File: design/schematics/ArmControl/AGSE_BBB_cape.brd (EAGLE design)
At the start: 71.8 x 54.6 mm, 53 parts, among them Q1 PFET-FQP27P06, Q2 PFET-FQP27P06, Q3 NFET-FQP30N06L, Q4 NFET-FQP30N06L, Q5 PFET-FQP27P06, Q6 PFET-FQP27P06, Q7 NFET-FQP30N06L, Q8 NFET-FQP30N06L, U1 V_REG_LD1085D2

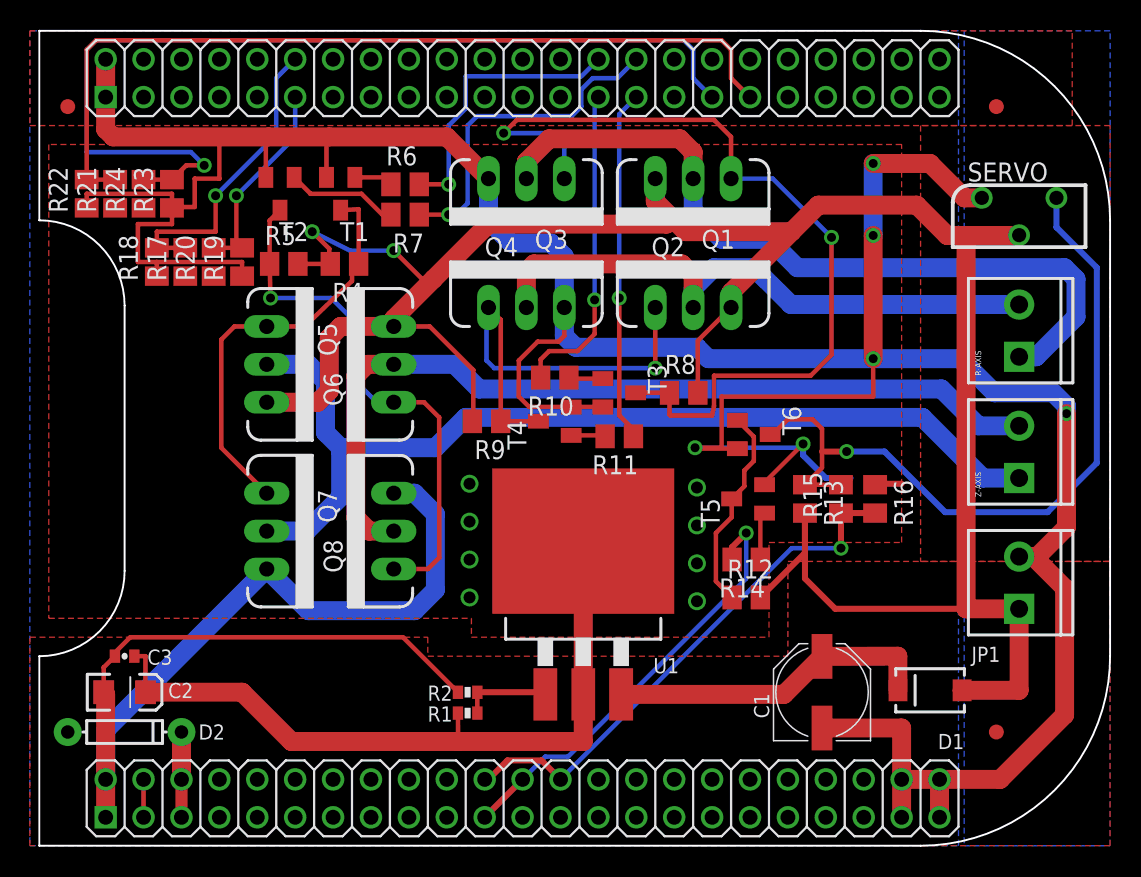
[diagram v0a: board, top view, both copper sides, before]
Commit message: routed the board.  Missing the encoder connectors.
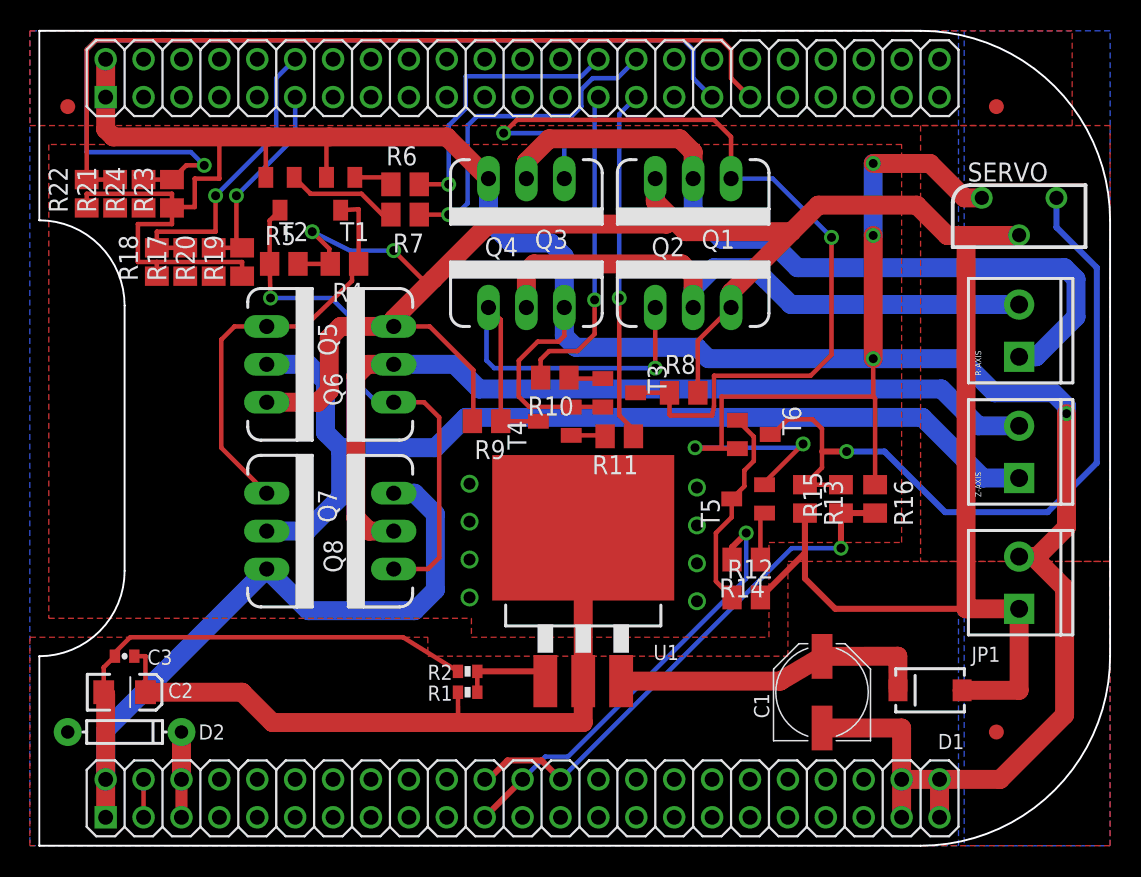
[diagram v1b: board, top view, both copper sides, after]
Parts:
- moved R1 1.40 mm to (45.8, 12.8)
- moved R2 1.40 mm to (45.8, 14.2)
- moved U1 0.89 mm to (53.6, 21.8)
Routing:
- net GND: track 325.6 -> 324.5 mm
- net VOUT: track 49.2 -> 48.4 mm
- net N$3: track 21.9 -> 21.3 mm
- net N$4: track 6.10 -> 6.61 mm
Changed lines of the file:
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@@
 <elements>
 <element name="U$1" library="adafruit" package="BEAGLEBONE_SHIELD" value="BEAGLEBONE_OUTLINE" x="2.54" y="57.15" smashed="yes" rot="R270"/>
-<element name="U1" library="SparkFun-PowerIC" package="D2PACK/A" value="V_REG_LD1085D2" x="53.594" y="20.955" smashed="yes">
-<attribute name="MANEX" value="140-0004281" x="53.594" y="20.955" size="1.778" layer="27" display="off"/>
-<attribute name="NAME" x="58.293" y="14.097" size="1.016" layer="25"/>
+<element name="U1" library="SparkFun-PowerIC" package="D2PACK/A" value="V_REG_LD1085D2" x="53.594" y="21.844" smashed="yes">
+<attribute name="MANEX" value="140-0004281" x="53.594" y="21.844" size="1.778" layer="27" display="off"/>
+<attribute name="NAME" x="58.293" y="14.986" size="1.016" layer="25"/>
 </element>
 <element name="JP1" library="SparkFun-Connectors" package="SCREWTERMINAL-3.5MM-2" value="M023.5MM" x="82.804" y="18.415" smashed="yes" rot="R90">
@@
 <attribute name="VALUE" x="21.844" y="8.763" size="0.4064" layer="27"/>
 </element>
-<element name="R1" library="SparkFun-Passives" package="0402-RES" value="370" x="45.847" y="11.43" smashed="yes" rot="R180">
-<attribute name="MANEX" value="110-0003316" x="45.847" y="11.43" size="1.778" layer="27" rot="R180" display="off"/>
-<attribute name="NAME" x="44.831" y="11.8745" size="1.016" layer="25" rot="R180"/>
-</element>
-<element name="R2" library="SparkFun-Passives" package="0402-RES" value="1.5k" x="45.847" y="12.827" smashed="yes">
-<attribute name="MANEX" value="110-0001936" x="45.847" y="12.827" size="1.778" layer="27" display="off"/>
+<element name="R1" library="SparkFun-Passives" package="0402-RES" value="370" x="45.847" y="12.827" smashed="yes" rot="R180">
+<attribute name="MANEX" value="110-0003316" x="45.847" y="12.827" size="1.778" layer="27" rot="R180" display="off"/>
 <attribute name="NAME" x="44.831" y="13.2715" size="1.016" layer="25" rot="R180"/>
+</element>
+<element name="R2" library="SparkFun-Passives" package="0402-RES" value="1.5k" x="45.847" y="14.224" smashed="yes">
+<attribute name="MANEX" value="110-0001936" x="45.847" y="14.224" size="1.778" layer="27" display="off"/>
+<attribute name="NAME" x="44.831" y="14.6685" size="1.016" layer="25" rot="R180"/>
 </element>
 <element name="FID1" library="SparkFun-Aesthetics" package="FIDUCIAL-1X2" value="FIDUCIAL1X2" x="19.05" y="52.07"/>
@@
 <wire x1="54.907" y1="31.943" x2="52.794" y2="31.943" width="0.3048" layer="1"/>
 <wire x1="52.794" y1="31.943" x2="52.789" y2="31.938" width="0.3048" layer="1"/>
-<wire x1="74.93" y1="26.797" x2="73.218" y2="26.797" width="0.4064" layer="1"/>
 <wire x1="73.218" y1="26.797" x2="73.152" y2="26.731" width="0.4064" layer="1"/>
 <wire x1="52.324" y1="38.608" x2="52.324" y2="42.037" width="1.27" layer="16"/>
@@
 <wire x1="21.59" y1="12.697" x2="21.59" y2="6.985" width="1.27" layer="1"/>
 <wire x1="21.59" y1="6.985" x2="21.59" y2="4.445" width="1.27" layer="1"/>
-<wire x1="45.197" y1="12.827" x2="41.514" y2="16.51" width="0.3048" layer="1"/>
+<wire x1="45.197" y1="14.224" x2="41.514" y2="16.51" width="0.3048" layer="1"/>
 <wire x1="41.514" y1="16.51" x2="23.241" y2="16.51" width="0.3048" layer="1"/>
 <wire x1="23.241" y1="16.51" x2="22.21" y2="15.479" width="0.3048" layer="1"/>
@@
 <wire x1="85.852" y1="11.303" x2="81.534" y2="6.985" width="1.27" layer="1"/>
 <wire x1="81.534" y1="6.985" x2="77.47" y2="6.985" width="1.27" layer="1"/>
-<wire x1="68.326" y1="29.464" x2="68.326" y2="28.702" width="0.4064" layer="16"/>
-<wire x1="68.326" y1="28.702" x2="69.85" y2="27.178" width="0.4064" layer="16"/>
-<wire x1="69.85" y1="27.178" x2="71.501" y2="27.178" width="0.4064" layer="16"/>
 <wire x1="80.304" y1="45.954" x2="79.141" y2="45.954" width="1.27" layer="1"/>
 <wire x1="79.141" y1="45.954" x2="76.835" y2="48.26" width="1.27" layer="1"/>
@@
 <wire x1="23.749" y1="44.196" x2="26.035" y2="44.196" width="0.3048" layer="1"/>
 <wire x1="26.035" y1="44.196" x2="26.035" y2="45.278" width="0.3048" layer="1"/>
-<wire x1="71.501" y1="27.178" x2="73.152" y2="26.731" width="0" layer="19" extent="1-16"/>
-<wire x1="42.291" y1="26.162" x2="49.276" y2="32.639" width="0" layer="19" extent="1-16"/>
+<wire x1="73.152" y1="26.731" x2="73.152" y2="32.512" width="0.3048" layer="1"/>
+<wire x1="73.152" y1="32.512" x2="73.025" y2="32.639" width="0.3048" layer="1"/>
 </signal>
 <signal name="N$3">
@@
 <wire x1="74.685" y1="12.954" x2="74.676" y2="15.24" width="1.27" layer="1"/>
 <wire x1="74.676" y1="15.24" x2="69.596" y2="15.227" width="1.27" layer="1"/>
-<wire x1="69.596" y1="15.227" x2="67.049" y2="12.68" width="1.27" layer="1"/>
-<wire x1="67.049" y1="12.68" x2="56.134" y2="12.68" width="1.27" layer="1"/>
+<wire x1="69.596" y1="15.227" x2="66.795" y2="13.569" width="1.27" layer="1"/>
+<wire x1="66.795" y1="13.569" x2="56.134" y2="13.569" width="1.27" layer="1"/>
 </signal>
 <signal name="5V">
@@
 <contactref element="U1" pad="1"/>
 <contactref element="R1" pad="1"/>
-<wire x1="46.497" y1="11.43" x2="46.497" y2="12.827" width="0.3048" layer="1"/>
-<wire x1="46.497" y1="12.827" x2="51.054" y2="12.827" width="0.4064" layer="1"/>
-<wire x1="51.054" y1="12.827" x2="51.054" y2="12.68" width="0.4064" layer="1"/>
+<wire x1="46.497" y1="12.827" x2="46.497" y2="14.224" width="0.3048" layer="1"/>
+<wire x1="46.497" y1="14.224" x2="51.054" y2="14.224" width="0.4064" layer="1"/>
+<wire x1="51.054" y1="14.224" x2="51.054" y2="13.569" width="0.4064" layer="1"/>
 </signal>
 <signal name="VOUT">
@@
 <contactref element="R1" pad="2"/>
 <contactref element="U1" pad="TAB"/>
-<wire x1="53.594" y1="12.68" x2="53.594" y2="22.955" width="1.27" layer="1"/>
+<wire x1="53.594" y1="13.569" x2="53.594" y2="23.844" width="1.27" layer="1"/>
 <via x="61.214" y="18.923" extent="1-16" drill="0.8"/>
 <via x="61.214" y="21.463" extent="1-16" drill="0.8"/>
@@
 <wire x1="24.26" y1="12.827" x2="24.257" y2="12.954" width="1.27" layer="1"/>
 <wire x1="24.26" y1="12.827" x2="30.734" y2="12.827" width="1.27" layer="1"/>
-<wire x1="30.734" y1="12.827" x2="34.036" y2="9.525" width="1.27" layer="1"/>
-<wire x1="34.036" y1="9.525" x2="45.212" y2="9.525" width="1.27" layer="1"/>
-<wire x1="45.212" y1="9.525" x2="53.594" y2="9.525" width="1.27" layer="1"/>
-<wire x1="53.594" y1="9.525" x2="53.594" y2="12.68" width="1.27" layer="1"/>
+<wire x1="30.734" y1="12.827" x2="32.766" y2="10.795" width="1.27" layer="1"/>
+<wire x1="32.766" y1="10.795" x2="45.212" y2="10.795" width="1.27" layer="1"/>
+<wire x1="45.212" y1="10.795" x2="53.594" y2="10.795" width="1.27" layer="1"/>
+<wire x1="53.594" y1="10.795" x2="53.594" y2="13.569" width="1.27" layer="1"/>
 <polygon width="0.3048" layer="1" thermals="no">
 <vertex x="17.78" y="49.53"/>
@@
 <vertex x="74.93" y="49.53"/>
 </polygon>
-<wire x1="45.197" y1="11.43" x2="45.212" y2="9.525" width="0.3048" layer="1"/>
+<wire x1="45.197" y1="12.827" x2="45.212" y2="10.795" width="0.3048" layer="1"/>
 <wire x1="23.51" y1="15.24" x2="24.257" y2="15.24" width="0.3048" layer="1"/>
 <wire x1="24.257" y1="15.24" x2="24.257" y2="12.954" width="0.3048" layer="1"/>

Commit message: routed the board, cleaned up the names and made ready for fab.
also added sparkfun's DRU for checking fab-ability
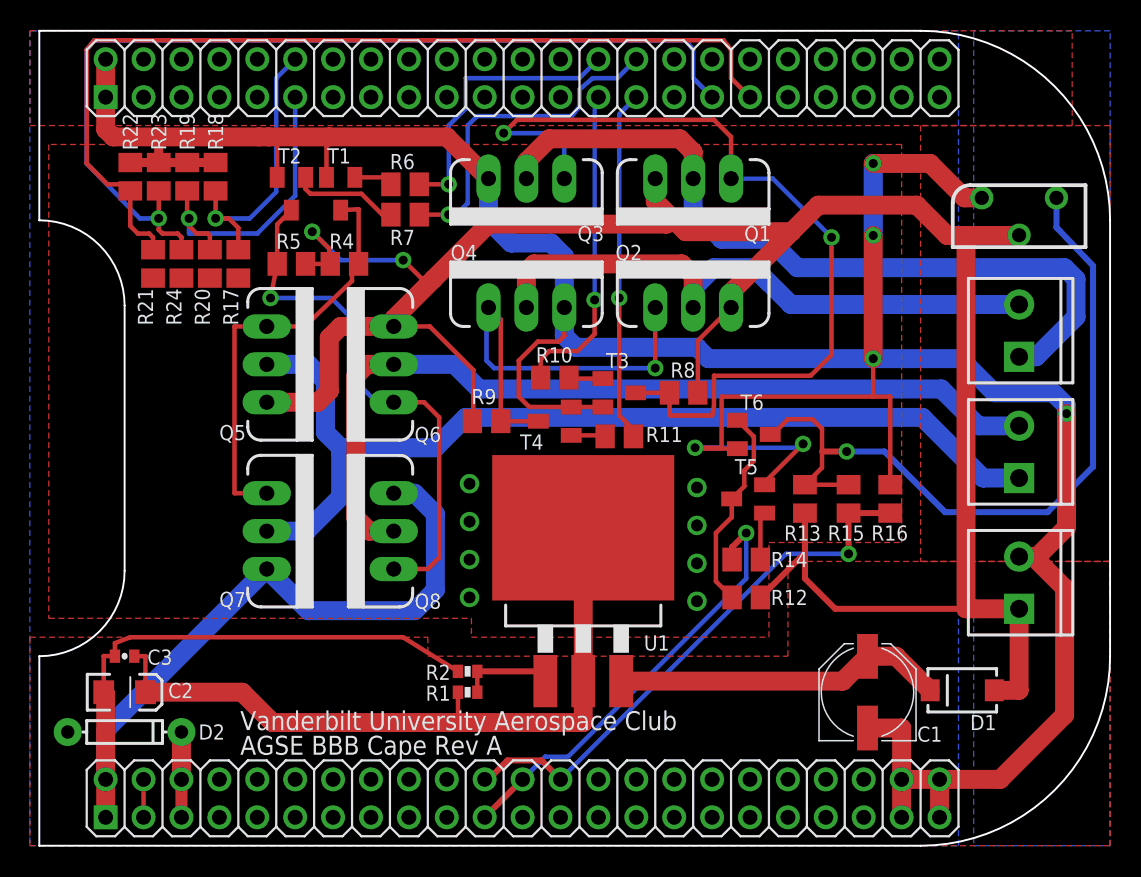
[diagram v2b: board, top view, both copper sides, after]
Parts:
- removed FID1, FID2, FID3: FIDUCIAL1X2, SparkFun-Aesthetics:FIDUCIAL-1X2
- moved R18 6.94 mm to (29.0, 47.4), turned to 270 degrees
- moved R19 6.80 mm to (27.1, 47.4), turned to 270 degrees
- moved R24 5.34 mm to (26.7, 41.5)
- moved R21 5.34 mm to (24.8, 41.5)
- moved R17 3.56 mm to (30.5, 41.5)
- moved R22 3.14 mm to (23.2, 47.4), turned to 270 degrees
- moved C1 3.05 mm to (72.6, 12.8)
- moved D1 2.16 mm to (79.0, 13.0)
- moved R23 1.45 mm to (25.1, 47.4), turned to 270 degrees
- moved R16 1.02 mm to (74.2, 25.8)
- moved T2 0.76 mm to (34.0, 46.2)
- moved R5 0.51 mm to (34.0, 41.5)
- moved R15 0.51 mm to (71.4, 25.8)
- moved R20 0.28 mm to (28.6, 41.5)
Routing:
- net GND: track 324.5 -> 293.7 mm
- net BBB_EQEP2B: track 14.0 -> 20.8 mm
- net BBB_EQEP1A: track 58.0 -> 64.0 mm
- net 12V: track 161.2 -> 158.8 mm
- net BBB_EQEP2A: track 20.7 -> 19.3 mm
- net BBB_RX: track 36.0 -> 37.2 mm
- net N$3: track 21.3 -> 22.3 mm
- net N$7: track 28.1 -> 28.6 mm
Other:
- board text added: "AGSE BBB Cape Rev A"
- board text added: "AX-12A"
- board text added: "R-Axis"
- board text added: "Vanderbilt University Aerospace Club"
- board text added: "Z-Axis"
- board text removed: "AGSE BBB Cape"
- board text removed: "R AXIS"
- board text removed: "Vanderbilt University"
- board text removed: "Z AXIS"
